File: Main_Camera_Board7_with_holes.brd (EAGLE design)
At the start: 127 x 44.2 mm, 8 parts

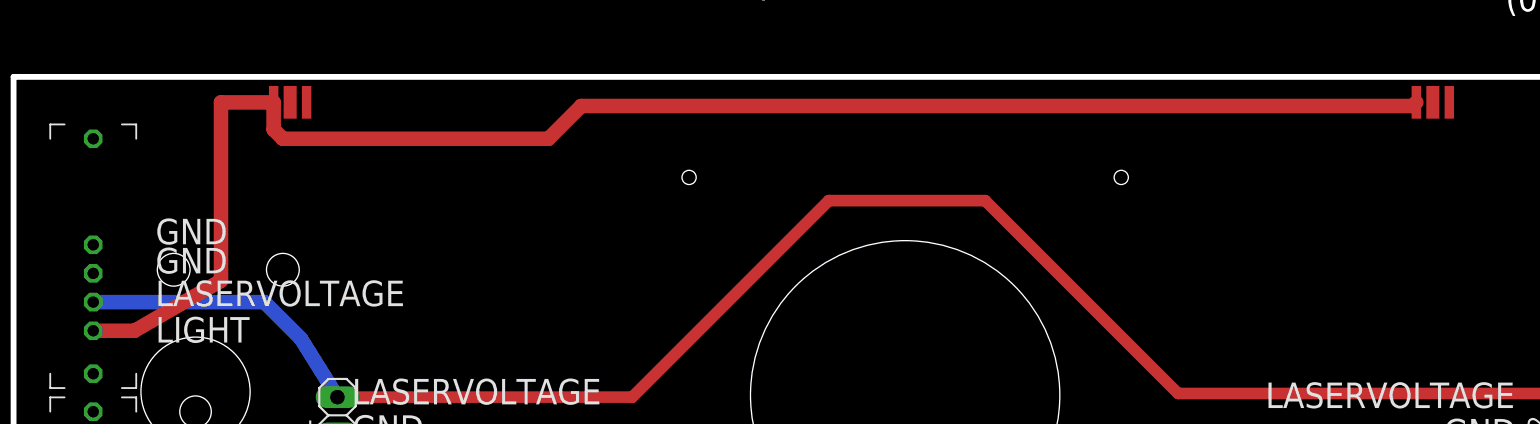
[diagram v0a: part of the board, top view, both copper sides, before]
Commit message: fixed airwire+updated readme
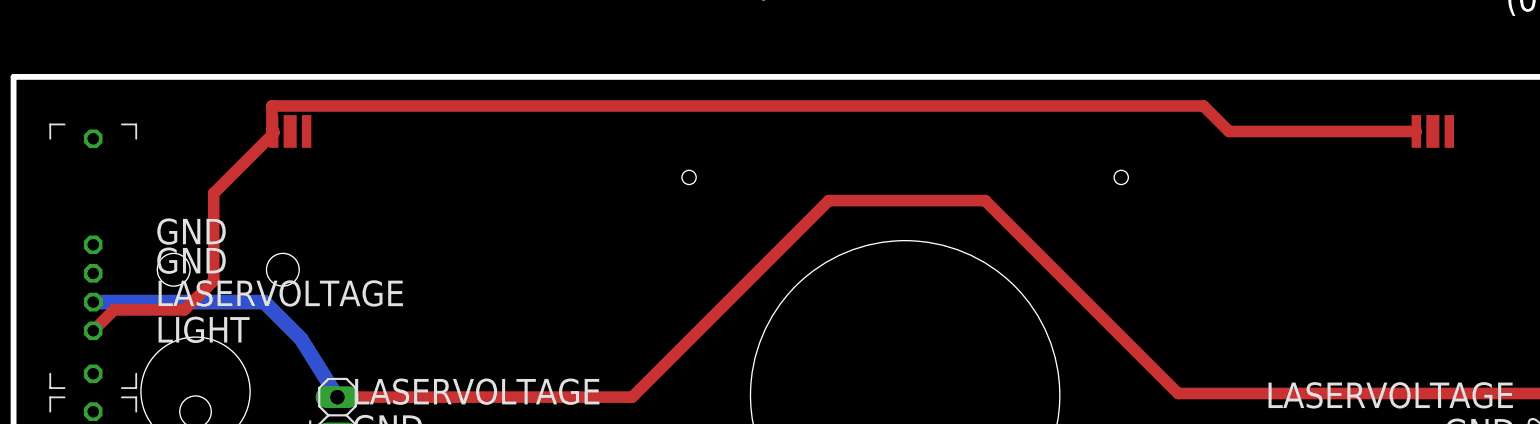
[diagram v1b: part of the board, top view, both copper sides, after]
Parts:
- moved U$2 2.03 mm to (15.5, 45.0)
- moved U$3 2.03 mm to (95.2, 45.0)
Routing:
- net LIGHT: track 109.0 -> 104.4 mm
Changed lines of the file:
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@@
 <elements>
 <element name="U$1" library="camera" package="ELP-USBFHD01M-L21" value="ELP-USBFHD01M-L21" x="58.42" y="25.4"/>
-<element name="U$2" library="camera" package="LED" value="LED" x="15.494" y="46.99"/>
-<element name="U$3" library="camera" package="LED" value="LED" x="95.25" y="46.99"/>
+<element name="U$2" library="camera" package="LED" value="LED" x="15.494" y="44.958"/>
+<element name="U$3" library="camera" package="LED" value="LED" x="95.25" y="44.958"/>
 <element name="U$4" library="camera" package="T2I" value="T21" x="1.75" y="44.45" rot="R270"/>
 <element name="U$5" library="camera" package="T2I" value="T21" x="1.75" y="25.4" rot="R270"/>
@@
 <contactref element="U$3" pad="P$2"/>
 <contactref element="U$4" pad="P$5"/>
-<wire x1="1.75" y1="31.05" x2="4.634" y2="31.05" width="1.016" layer="1"/>
-<wire x1="14.344" y1="46.99" x2="14.344" y2="45.092" width="1.016" layer="1"/>
-<wire x1="14.344" y1="45.092" x2="14.986" y2="44.45" width="1.016" layer="1"/>
-<wire x1="14.986" y1="44.45" x2="33.528" y2="44.45" width="1.016" layer="1"/>
-<wire x1="33.528" y1="44.45" x2="35.814" y2="46.736" width="1.016" layer="1"/>
-<wire x1="35.814" y1="46.736" x2="93.846" y2="46.736" width="1.016" layer="1"/>
-<wire x1="93.846" y1="46.736" x2="94.1" y2="46.99" width="1.016" layer="1"/>
-<wire x1="4.634" y1="31.05" x2="10.668" y2="34.544" width="1.016" layer="1"/>
-<wire x1="10.668" y1="34.544" x2="10.668" y2="46.99" width="1.016" layer="1"/>
-<wire x1="10.668" y1="46.99" x2="14.344" y2="46.99" width="1.016" layer="1"/>
+<wire x1="94.1" y1="44.958" x2="81.026" y2="44.958" width="0.8128" layer="1"/>
+<wire x1="81.026" y1="44.958" x2="79.248" y2="46.736" width="0.8128" layer="1"/>
+<wire x1="79.248" y1="46.736" x2="14.224" y2="46.736" width="0.8128" layer="1"/>
+<wire x1="14.224" y1="46.736" x2="14.224" y2="45.078" width="0.8128" layer="1"/>
+<wire x1="14.224" y1="45.078" x2="14.344" y2="44.958" width="0.8128" layer="1"/>
+<wire x1="14.344" y1="44.958" x2="14.344" y2="44.824" width="0.8128" layer="1"/>
+<wire x1="14.344" y1="44.824" x2="10.16" y2="40.64" width="0.8128" layer="1"/>
+<wire x1="3.212" y1="32.512" x2="1.75" y2="31.05" width="0.8128" layer="1"/>
+<wire x1="3.212" y1="32.512" x2="8.128" y2="32.512" width="0.8128" layer="1"/>
+<wire x1="8.128" y1="32.512" x2="10.16" y2="34.544" width="0.8128" layer="1"/>
+<wire x1="10.16" y1="34.544" x2="10.16" y2="40.64" width="0.8128" layer="1"/>
 </signal>
 </signals>

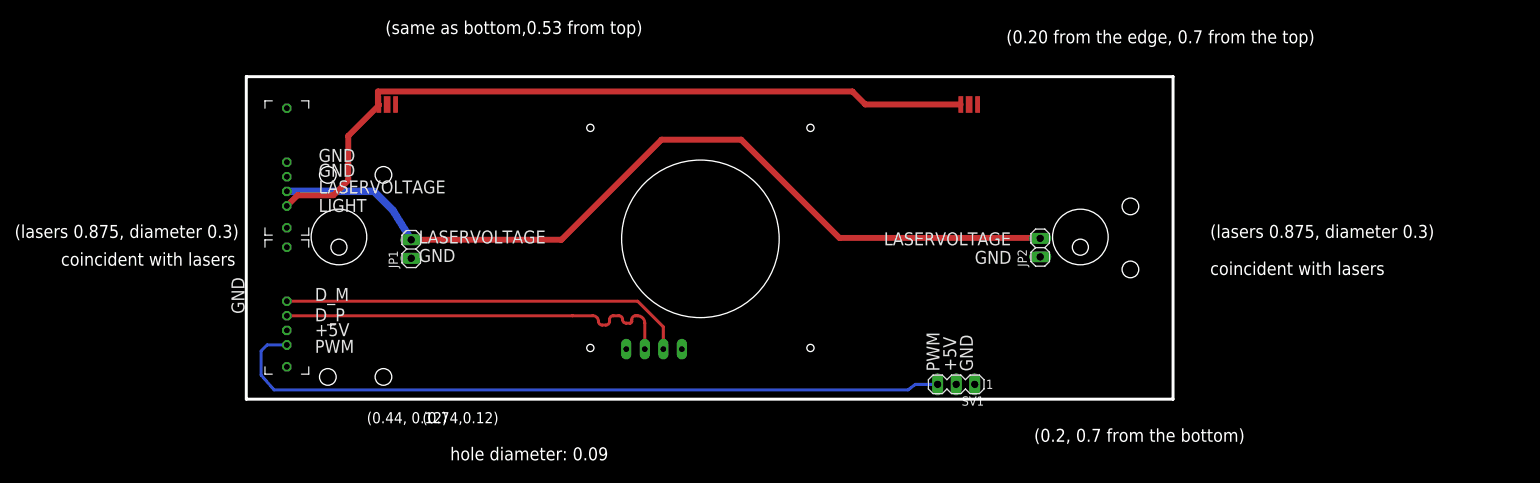
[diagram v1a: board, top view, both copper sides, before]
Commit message: made central camera hole larger, readjusted traces, fixed drc issues
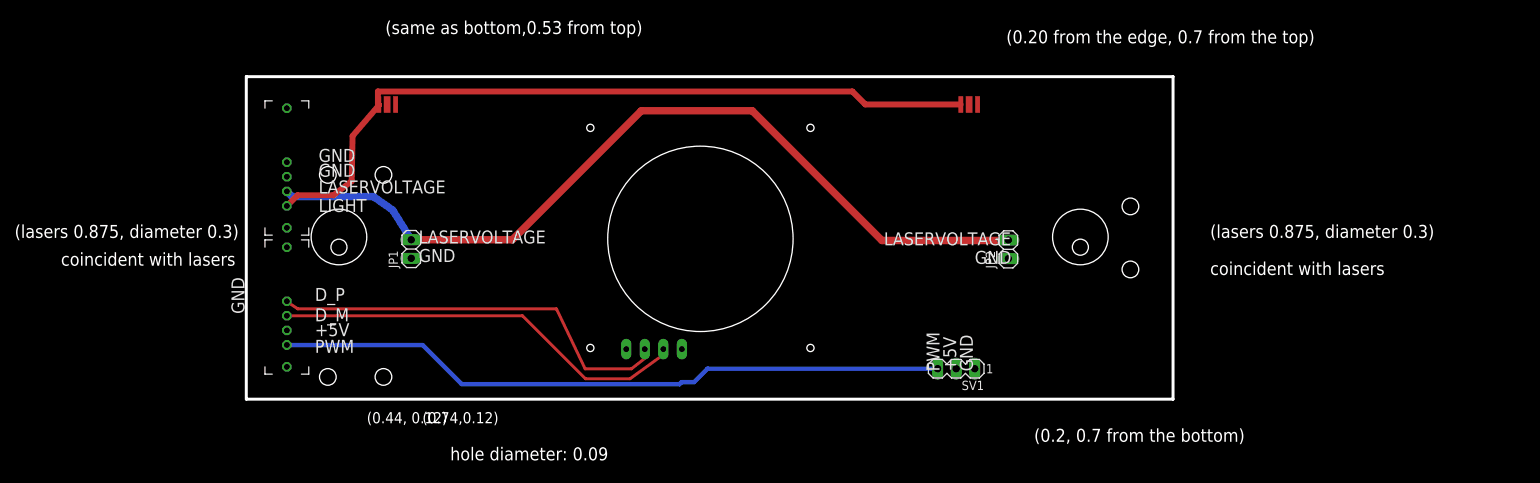
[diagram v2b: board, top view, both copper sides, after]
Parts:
- moved JP2 4.37 mm to (100.6, 25.1)
- moved SV1 2.14 mm to (93.5, 8.75)
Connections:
- net D_M: now also U$5.P$3; no longer U$5.P$2
- net D_P: now also U$5.P$2; no longer U$5.P$3
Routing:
- net PWM: track 101.1 -> 92.3 mm
- net LASER: track 118.1 -> 116.7 mm
- net D_P: track 55.2 -> 56.4 mm
- net D_M: track 56.1 -> 57.0 mm
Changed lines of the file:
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@@
 <setting verticaltext="up"/>
 </settings>
-<grid distance="0.08" unitdist="inch" unit="inch" style="lines" multiple="1" display="yes" altdistance="0.025" altunitdist="inch" altunit="inch"/>
+<grid distance="0.0015625" unitdist="inch" unit="inch" style="lines" multiple="1" display="yes" altdistance="0.025" altunitdist="inch" altunit="inch"/>
 <layers>
 <layer number="1" name="Top" color="4" fill="1" visible="yes" active="yes"/>
@@
 <text x="5.588" y="10.922" size="1.778" layer="25">PWM</text>
 <text x="5.588" y="13.208" size="1.778" layer="25">+5V</text>
-<text x="5.588" y="15.24" size="1.778" layer="25">D_P</text>
-<text x="5.588" y="18.034" size="1.778" layer="25">D_M</text>
+<text x="5.588" y="15.24" size="1.778" layer="25">D_M</text>
+<text x="5.588" y="18.034" size="1.778" layer="25">D_P</text>
 <text x="19.812" y="23.368" size="1.778" layer="25">GND</text>
 <text x="19.812" y="25.908" size="1.778" layer="25">LASERVOLTAGE</text>
@@
 <text x="96.012" y="23.114" size="1.778" layer="25">GND</text>
 <text x="83.566" y="25.654" size="1.778" layer="25">LASERVOLTAGE</text>
-<hole x="58.42" y="26.543" drill="21.59"/>
+<hole x="58.42" y="26.543" drill="25.4"/>
 <text x="24.13" y="-3.81" size="1.778" layer="20">hole diameter: 0.09</text>
 <text x="12.7" y="1.27" size="1.524" layer="20">(0.44, 0.12)</text>
@@
 <element name="U$5" library="camera" package="T2I" value="T21" x="1.75" y="25.4" rot="R270"/>
 <element name="JP1" library="pinhead" package="1X02" value="" x="18.796" y="25.146" rot="R90"/>
-<element name="JP2" library="pinhead" package="1X02" value="" x="104.986" y="25.338" rot="R90"/>
-<element name="SV1" library="con-lstb" package="MA03-1" value="" x="93.472" y="6.604" rot="R180">
-<attribute name="MF" value="" x="93.472" y="6.604" size="1.778" layer="27" rot="R180" display="off"/>
-<attribute name="OC_FARNELL" value="unknown" x="93.472" y="6.604" size="1.778" layer="27" rot="R180" display="off"/>
-<attribute name="MPN" value="" x="93.472" y="6.604" size="1.778" layer="27" rot="R180" display="off"/>
-<attribute name="OC_NEWARK" value="unknown" x="93.472" y="6.604" size="1.778" layer="27" rot="R180" display="off"/>
+<element name="JP2" library="pinhead" package="1X02" value="" x="100.620375" y="25.099875" rot="R90"/>
+<element name="SV1" library="con-lstb" package="MA03-1" value="" x="93.472" y="8.747125" rot="R180">
+<attribute name="MF" value="" x="93.472" y="8.747125" size="1.778" layer="27" rot="R180" display="off"/>
+<attribute name="OC_FARNELL" value="unknown" x="93.472" y="8.747125" size="1.778" layer="27" rot="R180" display="off"/>
+<attribute name="MPN" value="" x="93.472" y="8.747125" size="1.778" layer="27" rot="R180" display="off"/>
+<attribute name="OC_NEWARK" value="unknown" x="93.472" y="8.747125" size="1.778" layer="27" rot="R180" display="off"/>
 </element>
 </elements>
@@
 <signal name="D_M">
 <contactref element="U$1" pad="P$2"/>
-<contactref element="U$5" pad="P$2"/>
-<wire x1="1.75" y1="18" x2="49.818" y2="18" width="0.4064" layer="1"/>
-<wire x1="49.818" y1="18" x2="53.34" y2="14.478" width="0.4064" layer="1"/>
-<wire x1="53.34" y1="14.478" x2="53.34" y2="11.43" width="0.4064" layer="1"/>
+<contactref element="U$5" pad="P$3"/>
+<wire x1="53.34" y1="11.43" x2="53.34" y2="10.668" width="0.4064" layer="1"/>
+<wire x1="53.34" y1="10.668" x2="48.768" y2="7.366" width="0.4064" layer="1"/>
+<wire x1="1.75" y1="16" x2="34.038" y2="16" width="0.4064" layer="1"/>
+<wire x1="34.038" y1="16" x2="42.672" y2="7.366" width="0.4064" layer="1"/>
+<wire x1="42.672" y1="7.366" x2="48.768" y2="7.366" width="0.4064" layer="1"/>
 </signal>
 <signal name="D_P">
 <contactref element="U$1" pad="P$3"/>
-<contactref element="U$5" pad="P$3"/>
-<wire x1="1.75" y1="16" x2="40.892" y2="16" width="0.4064" layer="1"/>
-<wire x1="40.892" y1="16" x2="40.894" y2="16.002" width="0.4064" layer="1"/>
-<wire x1="40.894" y1="16.002" x2="43.688" y2="16.002" width="0.4064" layer="1"/>
-<wire x1="43.688" y1="16.002" x2="44.45" y2="15.24" width="0.4064" layer="1" curve="-90"/>
-<wire x1="44.45" y1="15.24" x2="44.958" y2="14.732" width="0.4064" layer="1" curve="90"/>
-<wire x1="44.958" y1="14.732" x2="45.466" y2="14.732" width="0.4064" layer="1"/>
-<wire x1="45.466" y1="14.732" x2="45.974" y2="15.24" width="0.4064" layer="1" curve="90"/>
-<wire x1="45.974" y1="15.24" x2="45.974" y2="15.494" width="0.4064" layer="1"/>
-<wire x1="45.974" y1="15.494" x2="46.482" y2="16.002" width="0.4064" layer="1" curve="-90"/>
-<wire x1="46.482" y1="16.002" x2="47.244" y2="16.002" width="0.4064" layer="1"/>
-<wire x1="47.244" y1="16.002" x2="47.752" y2="15.494" width="0.4064" layer="1" curve="-90"/>
-<wire x1="47.752" y1="15.494" x2="48.26" y2="14.986" width="0.4064" layer="1" curve="90"/>
-<wire x1="48.26" y1="14.986" x2="48.768" y2="14.986" width="0.4064" layer="1"/>
-<wire x1="48.768" y1="14.986" x2="49.022" y2="15.24" width="0.4064" layer="1" curve="90"/>
-<wire x1="49.022" y1="15.24" x2="49.022" y2="15.494" width="0.4064" layer="1"/>
-<wire x1="49.022" y1="15.494" x2="49.53" y2="16.002" width="0.4064" layer="1" curve="-90"/>
-<wire x1="49.53" y1="16.002" x2="49.784" y2="16.002" width="0.4064" layer="1"/>
-<wire x1="49.784" y1="16.002" x2="50.8" y2="14.986" width="0.4064" layer="1" curve="-90"/>
-<wire x1="50.8" y1="14.986" x2="50.8" y2="11.43" width="0.4064" layer="1"/>
+<contactref element="U$5" pad="P$2"/>
+<wire x1="1.75" y1="18" x2="1.75" y2="17.935" width="0.4064" layer="1"/>
+<wire x1="1.75" y1="17.935" x2="3.254375" y2="16.9465625" width="0.4064" layer="1"/>
+<wire x1="3.254375" y1="16.9465625" x2="38.6953125" y2="16.9465625" width="0.4064" layer="1"/>
+<wire x1="38.6953125" y1="16.9465625" x2="42.624375" y2="8.73125" width="0.4064" layer="1"/>
+<wire x1="42.624375" y1="8.73125" x2="48.974375" y2="8.73125" width="0.4064" layer="1"/>
+<wire x1="48.974375" y1="8.73125" x2="50.8" y2="10.16" width="0.4064" layer="1"/>
+<wire x1="50.8" y1="10.16" x2="50.8" y2="11.43" width="0.4064" layer="1"/>
 </signal>
 <signal name="N$2">
@@
 <contactref element="JP2" pad="2"/>
 <contactref element="U$4" pad="P$4"/>
-<wire x1="1.75" y1="33.05" x2="13.686" y2="33.05" width="1.016" layer="16"/>
-<wire x1="13.686" y1="33.05" x2="16.256" y2="30.48" width="1.016" layer="16"/>
+<wire x1="13.606625" y1="32.335625" x2="16.256" y2="30.48" width="1.016" layer="16"/>
 <wire x1="16.256" y1="30.48" x2="18.796" y2="26.416" width="1.016" layer="16"/>
-<wire x1="104.794" y1="26.416" x2="104.986" y2="26.608" width="1.016" layer="1"/>
-<wire x1="18.796" y1="26.416" x2="39.37" y2="26.416" width="0.8128" layer="1"/>
-<wire x1="39.37" y1="26.416" x2="53.086" y2="40.132" width="0.8128" layer="1"/>
-<wire x1="53.086" y1="40.132" x2="64.008" y2="40.132" width="0.8128" layer="1"/>
-<wire x1="64.008" y1="40.132" x2="77.47" y2="26.67" width="0.8128" layer="1"/>
-<wire x1="77.47" y1="26.67" x2="104.924" y2="26.67" width="0.8128" layer="1"/>
-<wire x1="104.924" y1="26.67" x2="104.986" y2="26.608" width="0.8128" layer="1"/>
+<wire x1="13.606625" y1="32.335625" x2="2.464375" y2="32.335625" width="1.016" layer="16"/>
+<wire x1="2.464375" y1="32.335625" x2="1.75" y2="33.05" width="1.016" layer="16"/>
+<wire x1="18.796" y1="26.416" x2="32.6469375" y2="26.416" width="1.016" layer="1"/>
+<wire x1="32.6469375" y1="26.416" x2="50.32375" y2="44.0928125" width="1.016" layer="1"/>
+<wire x1="50.32375" y1="44.0928125" x2="65.5240625" y2="44.0928125" width="1.016" layer="1"/>
+<wire x1="65.5240625" y1="44.0928125" x2="83.3040625" y2="26.3128125" width="1.016" layer="1"/>
+<wire x1="83.3040625" y1="26.3128125" x2="100.5633125" y2="26.3128125" width="1.016" layer="1"/>
+<wire x1="100.5633125" y1="26.3128125" x2="100.620375" y2="26.369875" width="1.016" layer="1"/>
 </signal>
 <signal name="N$7">
@@
 <contactref element="SV1" pad="3"/>
 <contactref element="U$5" pad="P$5"/>
-<wire x1="1.75" y1="12" x2="-0.954" y2="12" width="0.4064" layer="16"/>
-<wire x1="-0.954" y1="12" x2="-1.778" y2="11.176" width="0.4064" layer="16"/>
-<wire x1="-1.778" y1="7.874" x2="-1.778" y2="11.176" width="0.4064" layer="16"/>
-<wire x1="-1.778" y1="7.874" x2="0" y2="5.842" width="0.4064" layer="16"/>
-<wire x1="0" y1="5.842" x2="86.868" y2="5.842" width="0.4064" layer="16"/>
-<wire x1="86.868" y1="5.842" x2="87.884" y2="6.604" width="0.4064" layer="16"/>
-<wire x1="87.884" y1="6.604" x2="90.932" y2="6.604" width="0.4064" layer="16"/>
+<wire x1="90.932" y1="8.747125" x2="59.388375" y2="8.747125" width="0.6096" layer="16"/>
+<wire x1="59.388375" y1="8.747125" x2="57.546875" y2="6.905625" width="0.6096" layer="16"/>
+<wire x1="57.546875" y1="6.905625" x2="55.8403125" y2="6.905625" width="0.6096" layer="16"/>
+<wire x1="55.8403125" y1="6.905625" x2="55.5625" y2="6.6278125" width="0.6096" layer="16"/>
+<wire x1="55.5625" y1="6.6278125" x2="25.7175" y2="6.6278125" width="0.6096" layer="16"/>
+<wire x1="25.7175" y1="6.6278125" x2="20.3596875" y2="11.985625" width="0.6096" layer="16"/>
+<wire x1="20.3596875" y1="11.985625" x2="1.764375" y2="11.985625" width="0.6096" layer="16"/>
+<wire x1="1.764375" y1="11.985625" x2="1.75" y2="12" width="0.6096" layer="16"/>
 </signal>
 <signal name="LIGHT">
@@
 <wire x1="14.224" y1="45.078" x2="14.344" y2="44.958" width="0.8128" layer="1"/>
 <wire x1="14.344" y1="44.958" x2="14.344" y2="44.824" width="0.8128" layer="1"/>
-<wire x1="14.344" y1="44.824" x2="10.16" y2="40.64" width="0.8128" layer="1"/>
+<wire x1="14.344" y1="44.824" x2="10.7553125" y2="40.64" width="0.8128" layer="1"/>
 <wire x1="3.212" y1="32.512" x2="1.75" y2="31.05" width="0.8128" layer="1"/>
 <wire x1="3.212" y1="32.512" x2="8.128" y2="32.512" width="0.8128" layer="1"/>
-<wire x1="8.128" y1="32.512" x2="10.16" y2="34.544" width="0.8128" layer="1"/>
-<wire x1="10.16" y1="34.544" x2="10.16" y2="40.64" width="0.8128" layer="1"/>
+<wire x1="8.128" y1="32.512" x2="10.63625" y2="34.464625" width="0.8128" layer="1"/>
+<wire x1="10.63625" y1="34.464625" x2="10.7553125" y2="40.64" width="0.8128" layer="1"/>
 </signal>
 </signals>
